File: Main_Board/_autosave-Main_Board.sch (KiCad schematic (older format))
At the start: 68 parts, among them IC1 AZ1085CD-3.3TRG1, J1 PJ-037A, U1 STM32L152ZCTx, U2 LM386, Y1 ABM10W-16.0000MHZ-4-B1U-T3

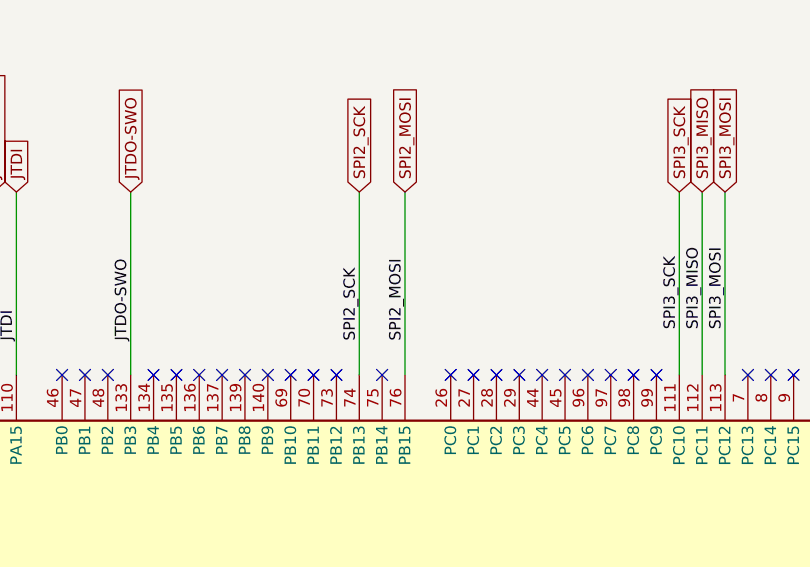
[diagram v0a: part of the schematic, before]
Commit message: 'switched uart'
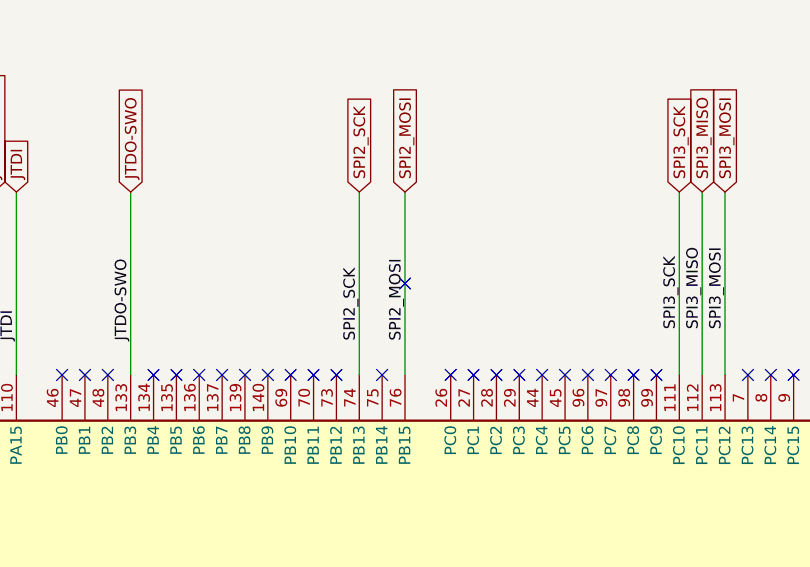
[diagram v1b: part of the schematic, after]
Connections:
- no-connect marks 84 -> 85
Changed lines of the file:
@@
 	20000 4550 20000 3900
 NoConn ~ 17800 4550
+NoConn ~ 18100 4150
 $EndSCHEMATC
